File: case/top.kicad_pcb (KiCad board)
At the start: 2 copper layers, 134.3 x 93.7 mm, 27 parts, among them SW1 SW_PUSH, SW10 SW_PUSH, SW11 SW_PUSH, SW12 SW_PUSH, SW13 SW_PUSH, SW14 SW_PUSH, SW15 SW_PUSH, SW16 SW_PUSH, SW17 SW_PUSH, SW18 SW_PUSH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

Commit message: update case files
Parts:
- moved H1 2.02 mm to (107.8, 76.5)
- moved H2 2.02 mm to (178.8, 125.0)
- moved H3 2.02 mm to (87.8, 95.5)
- moved H4 2.02 mm to (127.2, 111.0)
- moved H5 2.02 mm to (165.2, 79.0)
- moved SW1 2.02 mm to (97.8, 75.0)
- moved SW10 2.02 mm to (173.8, 88.5)
- moved SW11 2.02 mm to (97.8, 113.0)
- moved SW12 2.02 mm to (116.8, 105.0)
- moved SW13 2.02 mm to (135.8, 101.0)
- moved SW14 2.02 mm to (154.8, 105.0)
- moved SW15 2.02 mm to (173.8, 107.5)
- moved SW16 2.02 mm to (78.8, 86.0)
- moved SW17 2.02 mm to (78.8, 105.0)
- moved SW2 2.02 mm to (116.8, 67.0)
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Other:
- board size 134.3 x 93.7 mm -> 135 x 95.7 mm

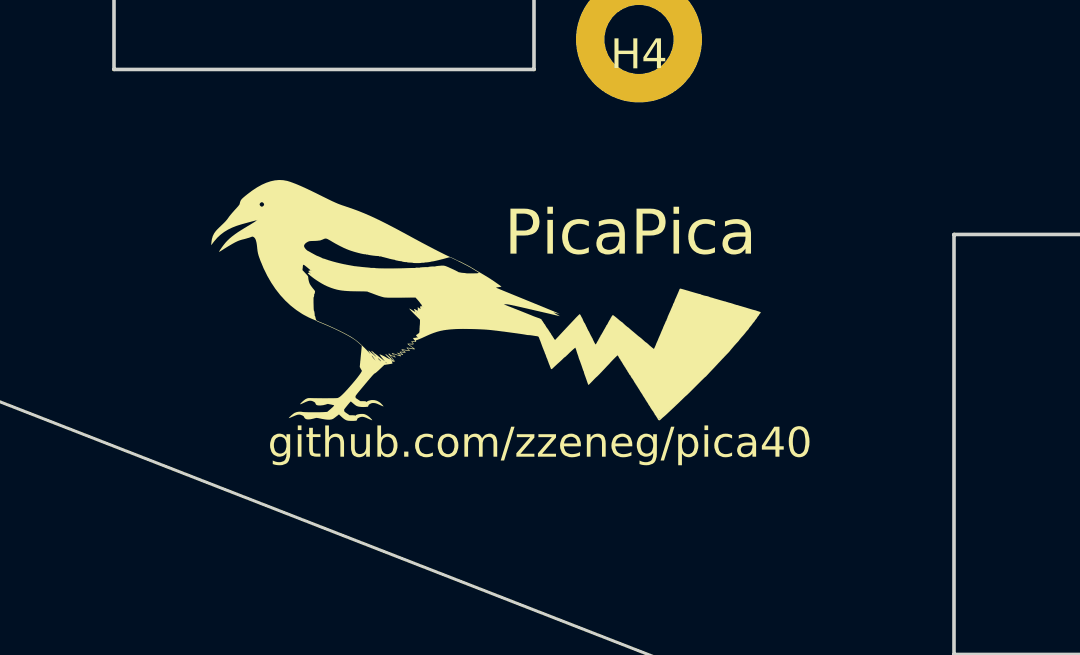
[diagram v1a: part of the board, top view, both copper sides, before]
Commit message: remove logos from top
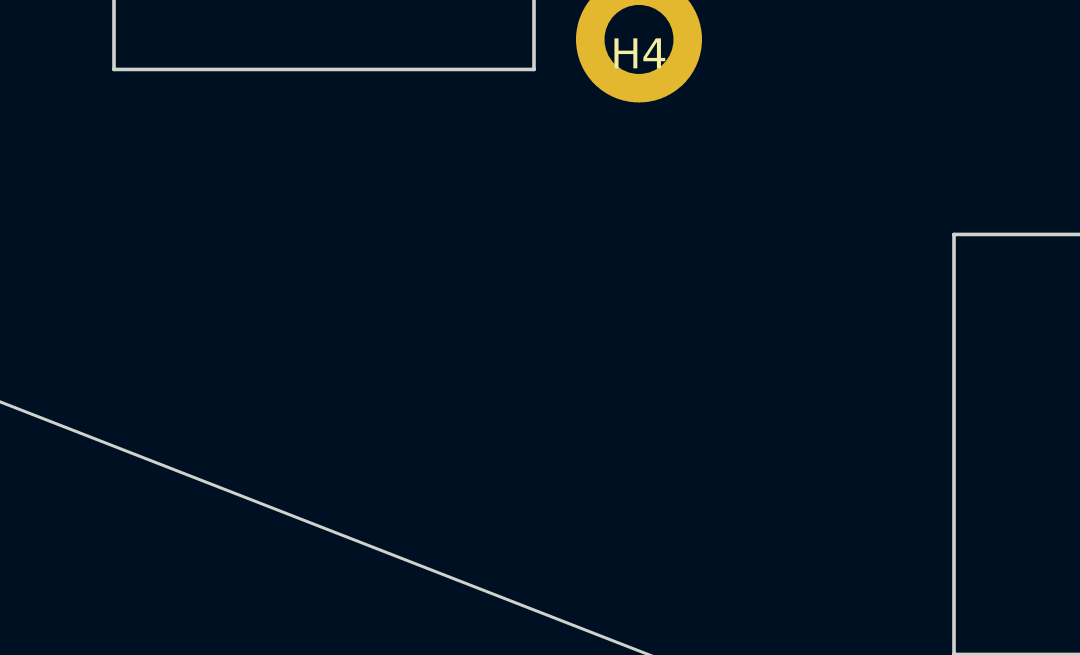
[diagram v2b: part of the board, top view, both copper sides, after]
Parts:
- removed G***: LOGO, pica:logo
- removed G***: LOGO, pica:logo_mirror
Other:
- board text removed: "PicaPica"
- board text removed: "github.com/zzeneg/pica40"

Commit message: update case files
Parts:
- added G***: LOGO, pica:logo_mirror, F.Cu at (121.8, 112.1)
- added G***: LOGO, pica:logo, B.Cu at (121.8, 112.1)
- added RE1: RotaryEncoder_Switch, pica:EC11_Hole, F.Cu at (193.0, 95.2)
- H1, H2, H3, H4, H5: footprint kbd:M2_Hole_TH -> kbd:thread_m2
- moved H1 10.3 mm to (105.3, 66.5)
- moved H2 10.0 mm to (178.0, 115.0)
- moved H4 10.0 mm to (126.5, 101.0)
- moved H5 10.0 mm to (164.5, 69.0)
- moved SW10 10.0 mm to (173.0, 78.5)
- moved SW12 10.0 mm to (116.0, 95.0)
- moved SW13 10.0 mm to (135.0, 91.0)
- moved SW15 10.0 mm to (173.0, 97.5)
- moved SW18 10.0 mm to (144.0, 114.5)
- moved SW19 10.0 mm to (165.2, 117.2)
- moved SW2 10.0 mm to (116.0, 57.0)
- moved SW20 10.0 mm to (187.5, 121.0)
- moved SW3 10.0 mm to (135.0, 53.0)
- moved SW5 10.0 mm to (173.0, 59.5)
- moved SW7 10.0 mm to (116.0, 76.0)
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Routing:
- net empty: vias 0 -> 1
- added copper zone on B.Cu, net empty
- added copper zone on F.Cu, net empty
- removed copper zone on B.Cu, net (none)
- removed copper zone on F.Cu, net (none)
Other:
- board size 135 x 95.7 mm -> 137.8 x 95.7 mm
- board text added: "Pica40 v2"
- board text added: "github.com/zzeneg/pica40"

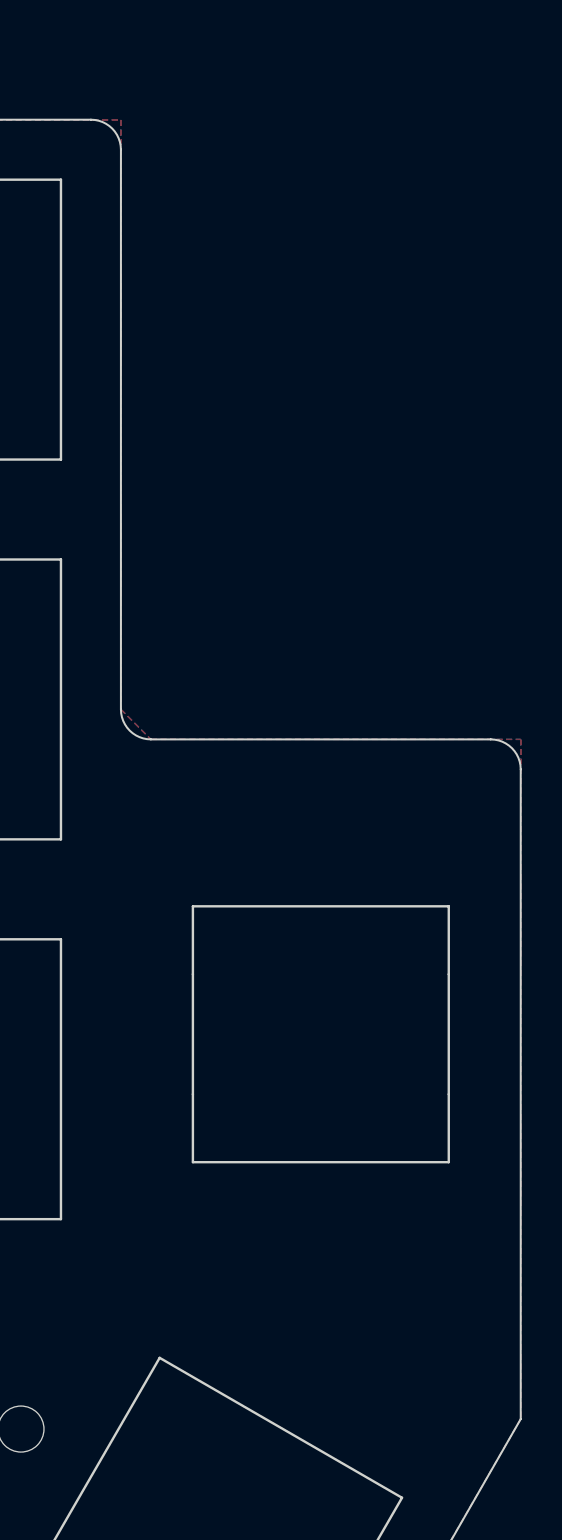
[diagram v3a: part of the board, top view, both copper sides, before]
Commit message: adjust top plate, add new cover in PCB style
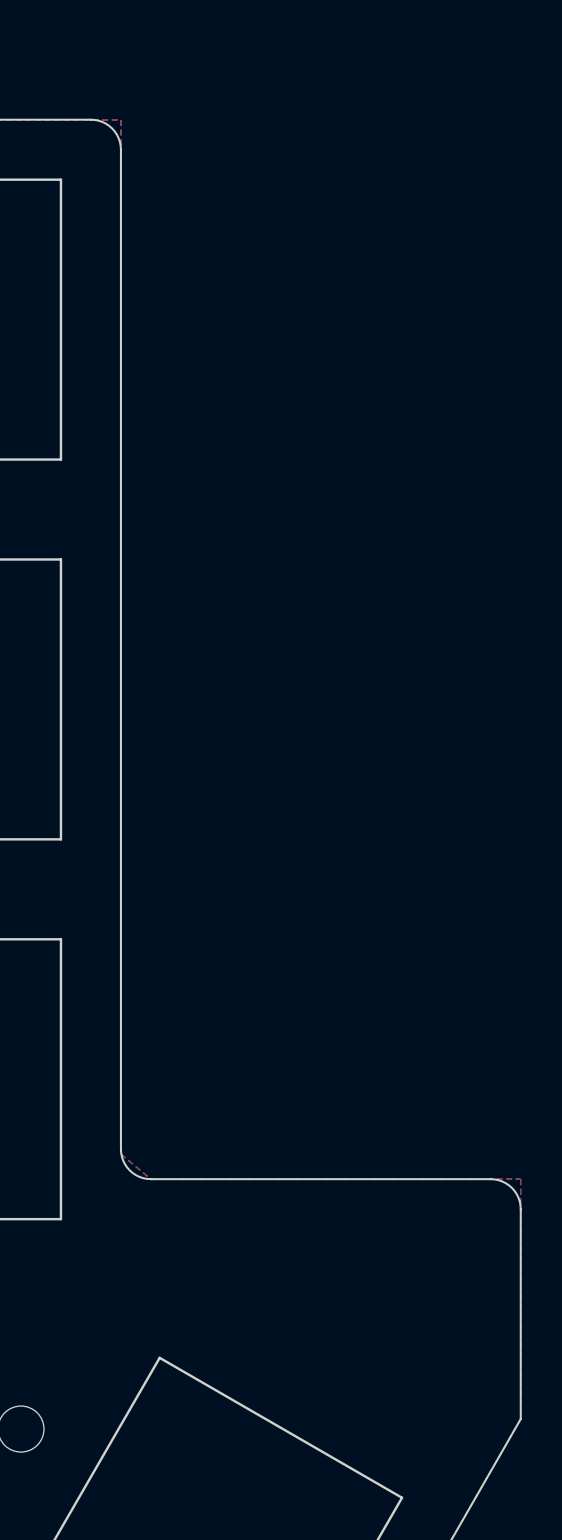
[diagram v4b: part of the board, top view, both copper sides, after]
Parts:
- removed RE1: RotaryEncoder_Switch, pica:EC11_Hole
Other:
- outline, holes or cut-outs redrawn
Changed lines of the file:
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@@
     (fp_line (start 9.525 -9.525) (end -9.525 -9.525) (layer "F.Fab") (width 0.15))
   )
-  (footprint "pica:EC11_Hole" (layer "F.Cu")
-    (at 193 95.25)
-    (property "Sheetfile" "full.kicad_sch")
-    (property "Sheetname" "")
-    (attr through_hole)
-    (fp_text reference "RE1" (at 0 7.7 unlocked) (layer "F.SilkS") hide
-      (effects (font (size 1 1) (thickness 0.15)))
-    )
-    (fp_text value "RotaryEncoder_Switch" (at 0 -7.3 unlocked) (layer "F.Fab") hide
-      (effects (font (size 1 1) (thickness 0.15)))
-    )
-    (fp_line (start 6.4 6.4) (end -6.4 6.4) (layer "Edge.Cuts") (width 0.12))
-    (fp_line (start -6.4 -6.4) (end -6.4 -3) (layer "Edge.Cuts") (width 0.12))
-    (fp_line (start 6.4 -3) (end 6.4 3) (layer "Edge.Cuts") (width 0.12))
-    (fp_line (start 6.4 -3) (end 6.4 -6.4) (layer "Edge.Cuts") (width 0.12))
-    (fp_line (start -6.4 -6.4) (end 6.4 -6.4) (layer "Edge.Cuts") (width 0.12))
-    (fp_line (start -6.4 -3) (end -6.4 3) (layer "Edge.Cuts") (width 0.12))
-    (fp_line (start 6.4 6.4) (end 6.4 3) (layer "Edge.Cuts") (width 0.12))
-    (fp_line (start -6.4 3) (end -6.4 6.4) (layer "Edge.Cuts") (width 0.12))
-  )
   (footprint "kbd:SW_Hole" (layer "F.Cu")
     (at 144 114.5)
@@
   (gr_line (start 107.5 47) (end 123.5 47) (layer "Edge.Cuts") (width 0.1))
   (gr_line (start 165.5 49.5) (end 181.5 49.5) (layer "Edge.Cuts") (width 0.1))
-  (gr_arc (start 184.5 80.5) (mid 183.43934 80.06066) (end 183 79) (layer "Edge.Cuts") (width 0.1))
+  (gr_arc (start 184.5 102.5) (mid 183.43934 102.06066) (end 183 101) (layer "Edge.Cuts") (width 0.1))
   (gr_arc (start 143.5 43) (mid 144.56066 43.43934) (end 145 44.5) (layer "Edge.Cuts") (width 0.1))
   (gr_line (start 106 48.5) (end 106 56.25) (layer "Edge.Cuts") (width 0.1))
   (gr_arc (start 162.5 47.5) (mid 163.401388 47.772918) (end 164 48.5) (layer "Edge.Cuts") (width 0.1))
-  (gr_arc (start 201.5 80.5) (mid 202.56066 80.93934) (end 203 82) (layer "Edge.Cuts") (width 0.1))
+  (gr_arc (start 201.5 102.5) (mid 202.56066 102.93934) (end 203 104) (layer "Edge.Cuts") (width 0.1))
   (gr_line (start 82.506854 73.299377) (end 66.518333 74.774974) (layer "Edge.Cuts") (width 0.1))
   (gr_arc (start 146.5 47.5) (mid 145.43934 47.06066) (end 145 46) (layer "Edge.Cuts") (width 0.1))
@@
   (gr_arc (start 83 61.224794) (mid 83.345246 60.129897) (end 84.363558 59.599769) (layer "Edge.Cuts") (width 0.1))
   (gr_arc (start 65.154775 76.4) (mid 65.500013 75.305096) (end 66.518333 74.774974) (layer "Edge.Cuts") (width 0.1))
-  (gr_line (start 184.5 80.5) (end 201.5 80.5) (layer "Edge.Cuts") (width 0.1))
+  (gr_line (start 184.5 102.5) (end 201.5 102.5) (layer "Edge.Cuts") (width 0.1))
   (gr_line (start 107.5 116) (end 134.5 124.5) (layer "Edge.Cuts") (width 0.1))
-  (gr_line (start 203 82) (end 203 114.5) (layer "Edge.Cuts") (width 0.1))
+  (gr_line (start 203 104) (end 203 114.5) (layer "Edge.Cuts") (width 0.1))
   (gr_arc (start 125 44.5) (mid 125.43934 43.43934) (end 126.5 43) (layer "Edge.Cuts") (width 0.1))
   (gr_line (start 104.425797 57.900232) (end 84.363558 59.599769) (layer "Edge.Cuts") (width 0.1))
@@
   (gr_arc (start 89.2 117.6) (mid 88.257339 117.211328) (end 87.8 116.3) (layer "Edge.Cuts") (width 0.1))
   (gr_line (start 187.5 138.5) (end 172 129.5) (layer "Edge.Cuts") (width 0.1))
-  (gr_line (start 183 51) (end 183 79) (layer "Edge.Cuts") (width 0.1))
+  (gr_line (start 183 51) (end 183 101) (layer "Edge.Cuts") (width 0.1))
   (gr_arc (start 165.5 49.5) (mid 164.598612 49.227082) (end 164 48.5) (layer "Edge.Cuts") (width 0.1))
   (gr_text "Pica40 v2" (at 125.55 117.85) (layer "B.SilkS")
@@
         (xy 165.25 49.5)
         (xy 182.999191 49.51189)
-        (xy 183 79)
-        (xy 184.5 80.5)
-        (xy 203 80.5)
+        (xy 183 101.25)
+        (xy 184.5 102.5)
+        (xy 203 102.5)
         (xy 203 114.5)
         (xy 188.75 139.25)
